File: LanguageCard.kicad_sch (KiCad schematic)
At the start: 29 parts, among them J1 Apple II Expansion Bus, U1 74LS86, U10 74LS06, U2 74LS08, U3 74LS175, U4 74LS32, U5 74LS08, U6 74LS08, U7 ROM F8, U8 6264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

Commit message: update symbols
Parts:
- U7: value ROM F8 -> ROM F8 (2716)
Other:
- moved on the sheet: D2, D4, JP1, R3, R5, R6, U10E, U4A

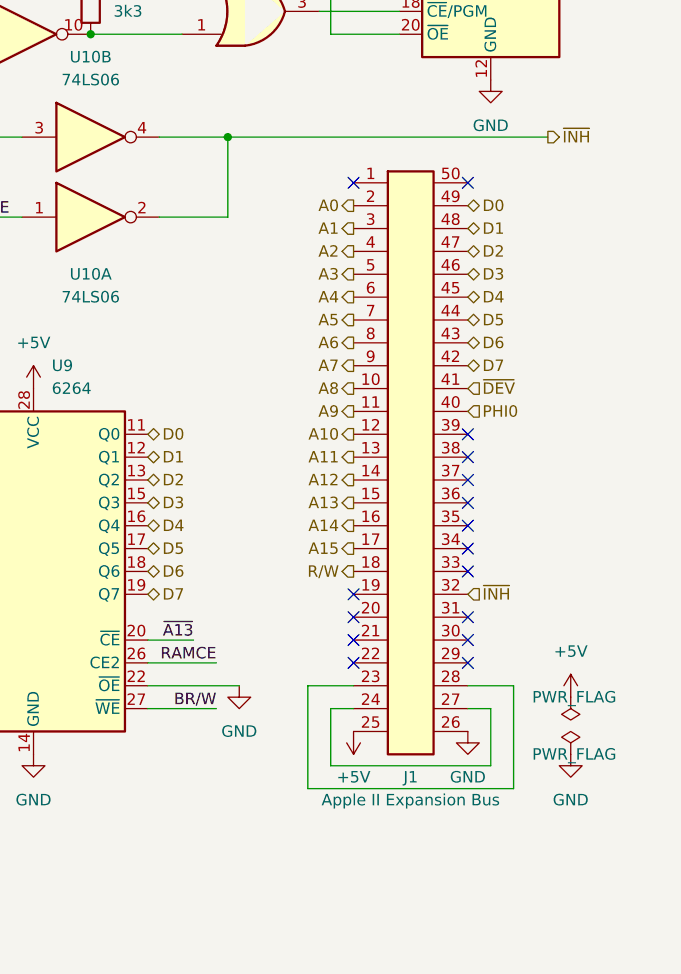
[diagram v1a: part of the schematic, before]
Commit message: just use a generic connector
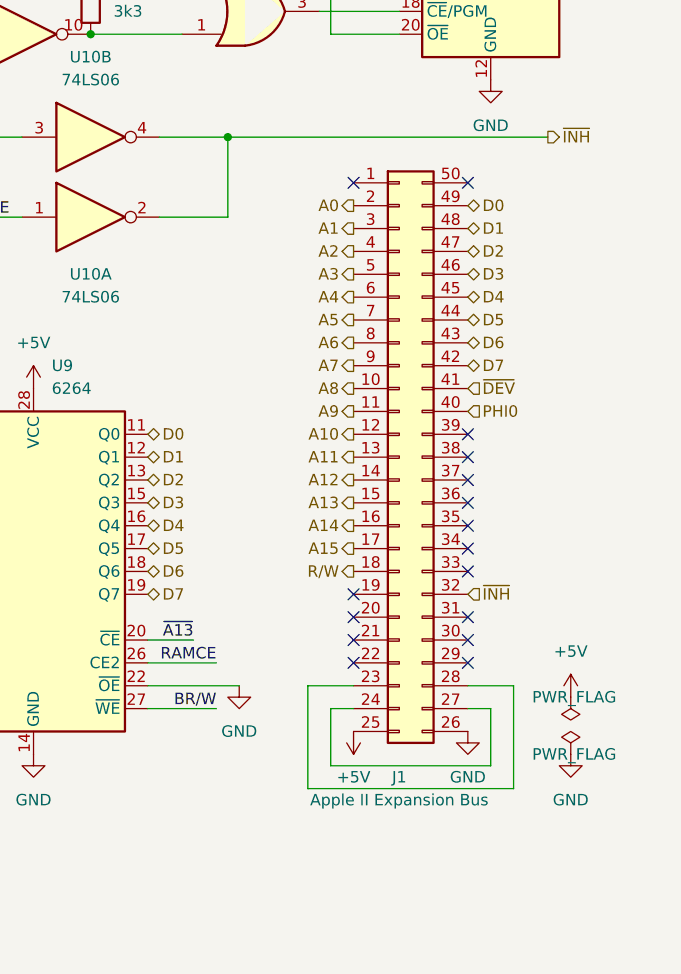
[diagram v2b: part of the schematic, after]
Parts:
- J1: symbol Apple II:Apple II Expansion Bus -> Connector_Generic:Conn_02x25_Counter_Clockwise; now in the parts list
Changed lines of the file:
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@@
   (paper "USLetter")
   (title_block
-    (rev "0")
+    (rev "1")
   )
   (junction (at 66.04 76.2) (diameter 0) (color 0 0 0 0)
@@
     (pin "1")
   )
-  (symbol (lib_id "Apple II:Apple II Expansion Bus") (at 241.3 132.08 0) (unit 1)
-    (in_bom no) (on_board yes) (fields_autoplaced)
-    (property "Reference" "J1" (id 0) (at 241.3 167.64 0))
-    (property "Value" "Apple II Expansion Bus" (id 1) (at 241.3 170.18 0))
-    (property "Footprint" "Apple2:Apple II Expansion Edge Connector" (id 2) (at 231.14 132.08 0)
-      (effects (font (size 1.27 1.27)) hide)
-    )
-    (property "Datasheet" "~" (id 3) (at 251.46 132.08 0)
-      (effects (font (size 1.27 1.27)) hide)
-    )
+  (symbol (lib_id "Connector_Generic:Conn_02x25_Counter_Clockwise") (at 240.03 132.08 0) (unit 1)
+    (in_bom yes) (on_board yes) (fields_autoplaced)
+    (property "Reference" "J1" (id 0) (at 240.03 167.64 0))
+    (property "Value" "Apple II Expansion Bus" (id 1) (at 240.03 170.18 0))
+    (property "Footprint" "Apple2:Apple II Expansion Edge Connector" (id 2) (at 240.03 132.08 0)
+      (effects (font (size 1.27 1.27)) hide)
+    )
+    (property "Datasheet" "~" (id 3) (at 240.03 132.08 0)
+      (effects (font (size 1.27 1.27)) hide)
+    )

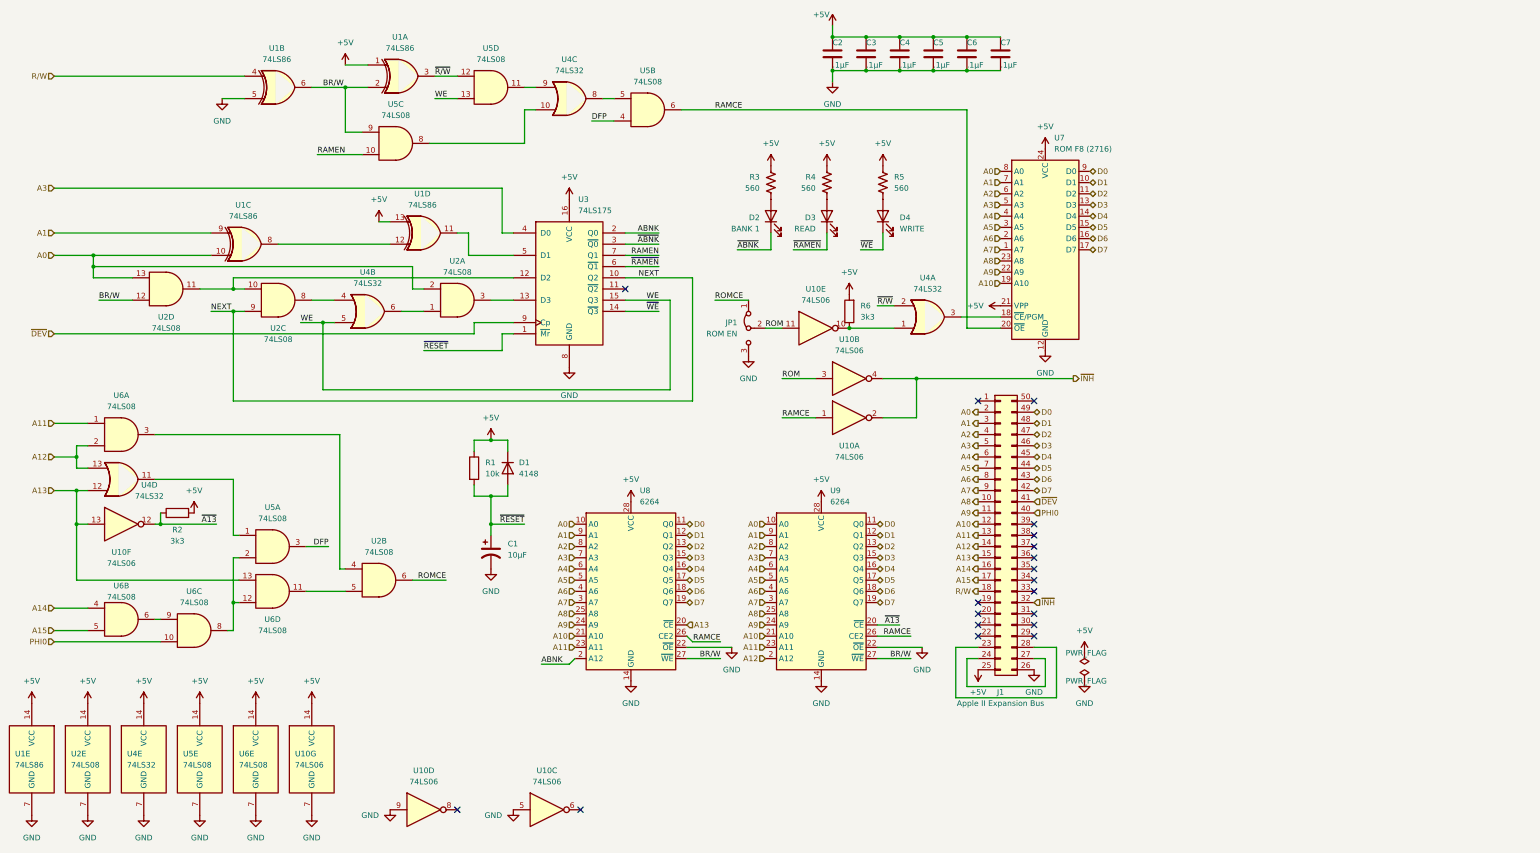
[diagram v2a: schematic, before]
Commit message: update to Kicad 7
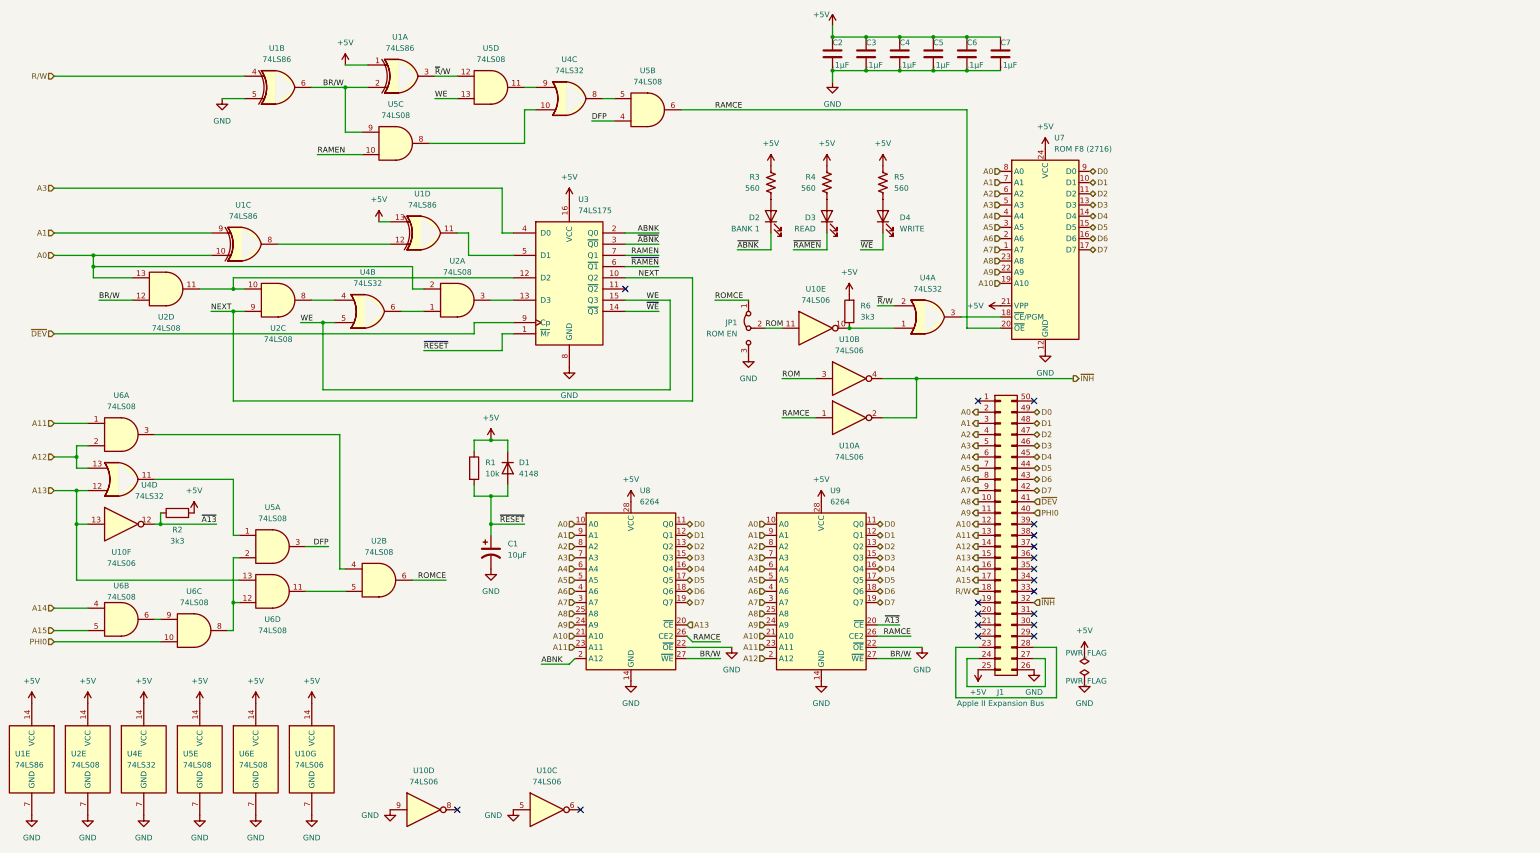
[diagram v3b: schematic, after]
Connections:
- net ~{R/W} renamed ~{R}/W

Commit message: Larger ROM, enable switch
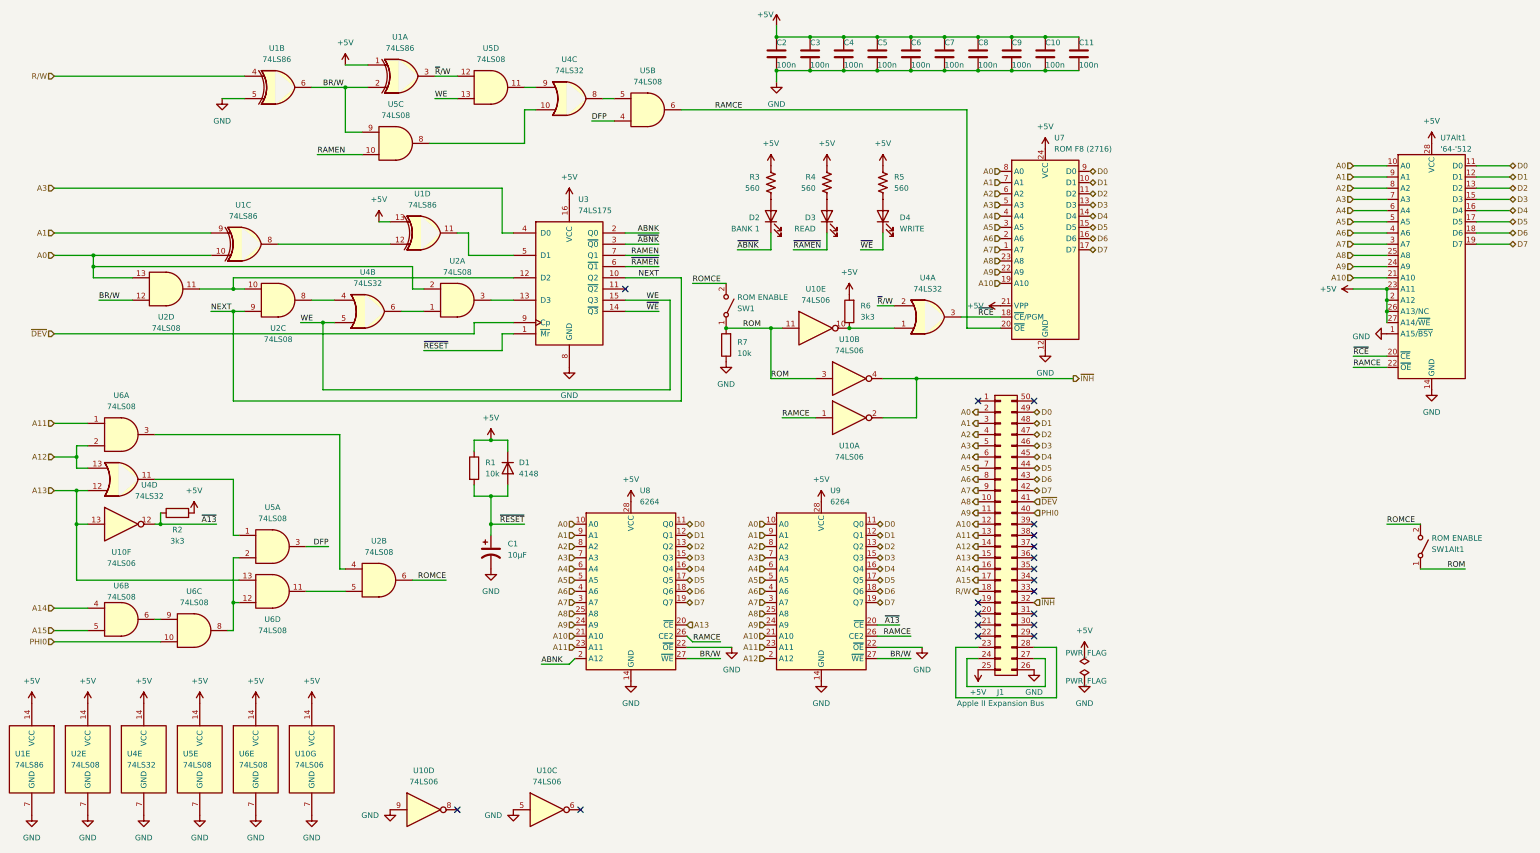
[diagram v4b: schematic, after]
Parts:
- removed JP1: ROM EN, Connector_PinHeader_2.54mm:PinHeader_1x03_P2.54mm_Vertical, symbol Jumper:Jumper_3_Bridged12
- added C10, C11, C8, C9: 100n, Capacitor_THT:C_Disc_D3.0mm_W1.6mm_P2.50mm, symbol Device:C
- added R7: 10k, Resistor_THT:R_Axial_DIN0207_L6.3mm_D2.5mm_P10.16mm_Horizontal, symbol Device:R
- added SW1: ROM ENABLE, MySwitch:SW_Lever_1P2T_Alcoswitch_AE101SD1, symbol Switch:SW_SPST
- added SW1Alt1: ROM ENABLE, Button_Switch_THT:SW_Lever_1P2T_NKK_GW12LxH, symbol Switch:SW_SPST
- added U7Alt1: '64-'512, Package_DIP:DIP-28_W15.24mm, symbol Memory_EPROM:27C512
- C1: footprint Capacitor_THT:CP_Radial_D8.0mm_P5.00mm -> Capacitor_THT:CP_Radial_D5.0mm_P2.50mm
- C2, C3, C4, C5, C6, C7: value .1μF -> 100n; footprint Capacitor_THT:C_Rect_L7.0mm_W2.0mm_P5.00mm -> Capacitor_THT:C_Disc_D3.0mm_W1.6mm_P2.50mm
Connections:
- net +5V: now also C10.1, C11.1, C8.1, C9.1, U7Alt1.2 (A12), U7Alt1.23 (A11), U7Alt1.26 (A13/NC), U7Alt1.27 (A14/~{WE}), U7Alt1.28 (VCC)
- net A0: now also U7Alt1.10 (A0)
- net A1: now also U7Alt1.9 (A1)
- net A10: now also U7Alt1.21 (A10)
- net A2: now also U7Alt1.8 (A2)
- net A3: now also U7Alt1.7 (A3)
- net A4: now also U7Alt1.6 (A4)
- net A5: now also U7Alt1.5 (A5)
- net A6: now also U7Alt1.4 (A6)
- net A7: now also U7Alt1.3 (A7)
- net A8: now also U7Alt1.25 (A8)
- net A9: now also U7Alt1.24 (A9)
- net D0: now also U7Alt1.11 (D0)
- net D1: now also U7Alt1.12 (D1)
- net D2: now also U7Alt1.13 (D2)
- net D3: now also U7Alt1.15 (D3)
- net D4: now also U7Alt1.16 (D4)
- net D5: now also U7Alt1.17 (D5)
- net D6: now also U7Alt1.18 (D6)
- net D7: now also U7Alt1.19 (D7)
- net GND: now also C10.2, C11.2, C8.2, C9.2, R7.1, U7Alt1.1 (A15/~{BSY}), U7Alt1.14 (GND)
- net RAMCE: now also U7Alt1.22 (~{OE})
- net ROM: now also R7.2, SW1.1 (A), SW1Alt1.1 (A)
- net ROMCE: now also SW1.2 (B), SW1Alt1.2 (B)
- net ~{RCE}: now reaches U4.3, U7.18 (~{CE}/PGM)
- net ~{RCE}: now also U7Alt1.20 (~{CE})
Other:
- moved on the sheet: C2, C3, C4, C5, C6, C7

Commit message: dual rom config, lots of tweaks
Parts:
- removed SW1Alt1: ROM ENABLE, Button_Switch_THT:SW_Lever_1P2T_NKK_GW12LxH, symbol Switch:SW_SPST
- added JP1: ROM Enable, Connector_PinHeader_2.54mm:PinHeader_2x03_P2.54mm_Vertical, symbol Connector_Generic:Conn_02x03_Odd_Even
- added JP2: DUAL ROM, Jumper:SolderJumper-2_P1.3mm_Open_RoundedPad1.0x1.5mm, symbol Jumper:SolderJumper_2_Open
- added JP3: SPST, Jumper:SolderJumper-2_P1.3mm_Open_RoundedPad1.0x1.5mm, symbol Jumper:SolderJumper_2_Open
- added R8: 10k, Resistor_THT:R_Axial_DIN0207_L6.3mm_D2.5mm_P10.16mm_Horizontal, symbol Device:R
- added unit 2 of SW1
- SW1: footprint MySwitch:SW_Lever_1P2T_Alcoswitch_AE101SD1 -> MySwitch:SW_Lever_2P2T_Alcoswitch_AE203SD1; symbol Switch:SW_SPST -> MySwitch:SW_DPDT_MSM_x2
- U7: value ROM F8 (2716) -> ROM F8 (2716/32)
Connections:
- net +5V: now also R8.2; no longer U7.21 (VPP), U7Alt1.23 (A11)
- net GND: now also SW1.3 (C), JP1.6 (Pin_6)
- net ROM renamed ROMEN
- net ROMEN: now also JP1.1 (Pin_1), JP2.2 (B), SW1.4 (A); no longer SW1.1 (A)
- net ROMCE renamed F8SEL
- net F8SEL: now also JP1.3 (Pin_3), JP3.1 (A), SW1.5 (B); no longer SW1.2 (B)
- net ~{RCE} renamed ~{ROMCE}
- new net ROMA11/VPP/~{WE}: JP1.4 (Pin_4), R8.1, SW1.2 (B), U7.21 (VPP), U7Alt1.23 (A11)
- new net ROMEN2: JP1.5 (Pin_5), JP2.1 (A), JP3.2 (B), SW1.6 (C)
- no-connect marks 19 -> 21
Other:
- moved on the sheet: J1, R6, R7, U10A, U10B, U10E, U4A, U7, U7Alt1, U9
